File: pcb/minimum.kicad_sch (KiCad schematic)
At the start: 32 parts, among them J1 DX07P024MJ1R1500, J2 Conn_01x02, U1 RP2040, U2 SCD4x, U3 W25Q16JVUXIQ, U4 XCL220, Y1 C2E-12.000-18-1020-X-R

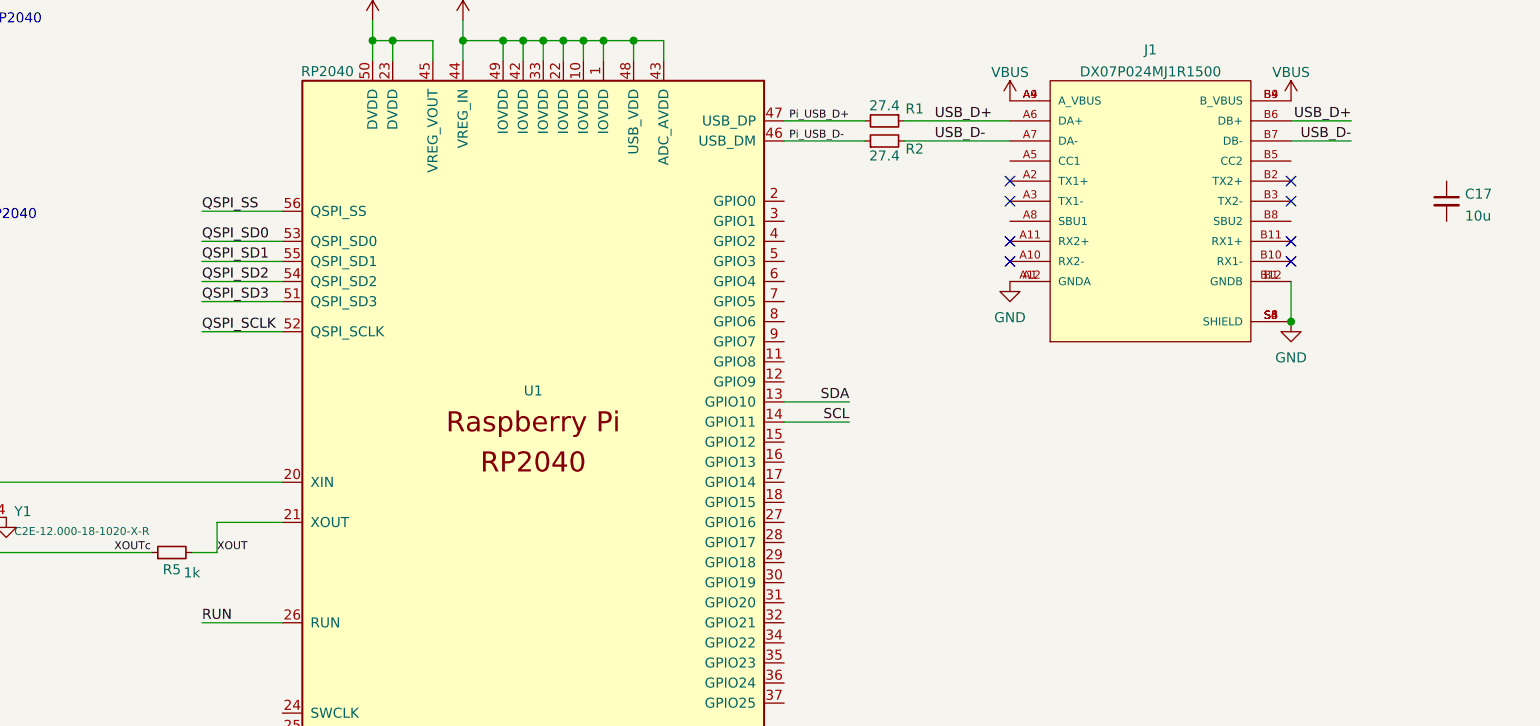
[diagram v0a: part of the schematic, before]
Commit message: routing VBUS
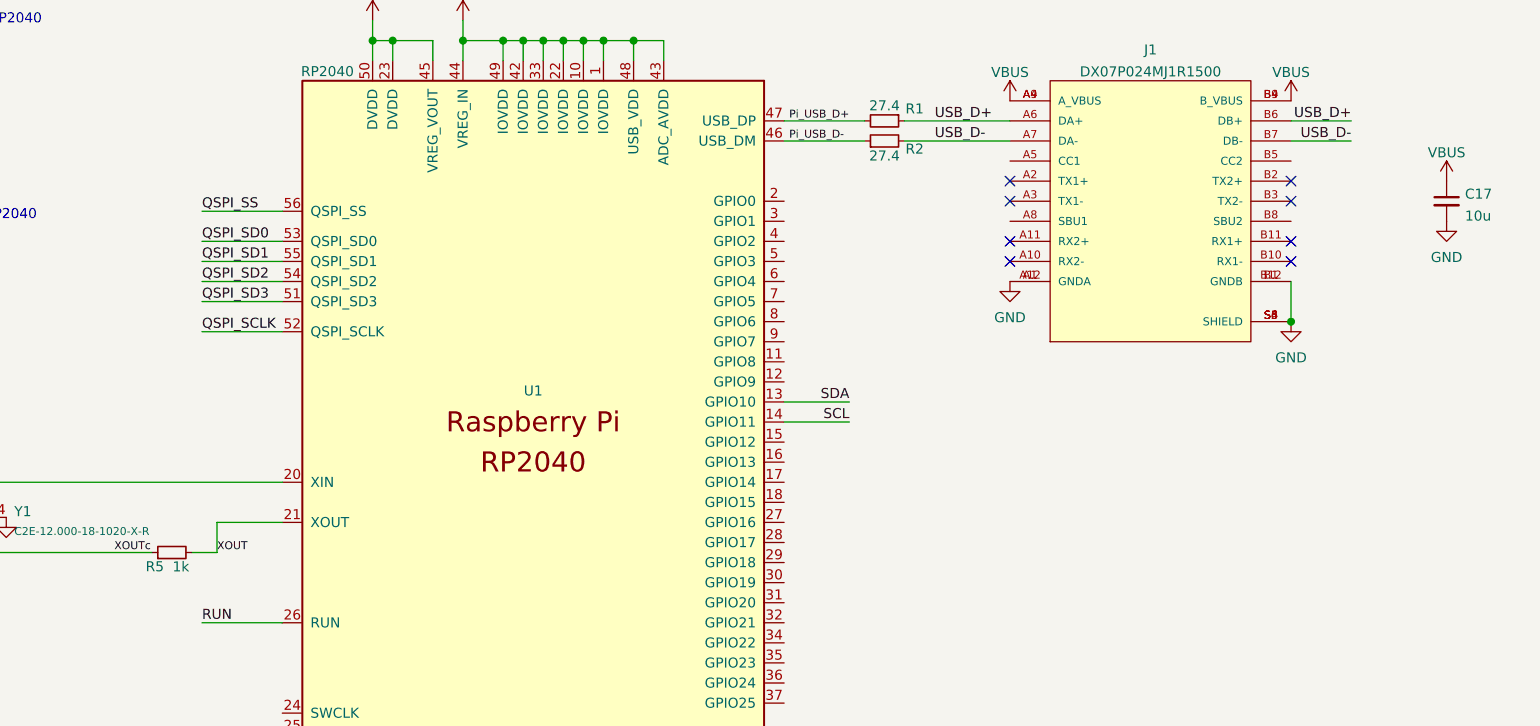
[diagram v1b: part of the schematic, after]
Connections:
- net GND: now also C17.2
- net VBUS: now also C17.1
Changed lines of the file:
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@@
   (symbol (lib_id "power:VBUS") (at 273.05 175.895 0) (unit 1)
     (in_bom yes) (on_board yes) (fields_autoplaced)
-    (property "Reference" "#PWR?" (id 0) (at 273.05 179.705 0)
+    (property "Reference" "#PWR0127" (id 0) (at 273.05 179.705 0)
       (effects (font (size 1.27 1.27)) hide)
     )
@@
     (pin "1")
   )
+  (symbol (lib_id "power:VBUS") (at 295.91 46.355 0) (unit 1)
+    (in_bom yes) (on_board yes) (fields_autoplaced)
+    (property "Reference" "#PWR?" (id 0) (at 295.91 50.165 0)
+      (effects (font (size 1.27 1.27)) hide)
+    )
+    (property "Value" "VBUS" (id 1) (at 295.91 42.7504 0))
+    (property "Footprint" "" (id 2) (at 295.91 46.355 0)
+      (effects (font (size 1.27 1.27)) hide)
+    )
+    (property "Datasheet" "" (id 3) (at 295.91 46.355 0)
+      (effects (font (size 1.27 1.27)) hide)
+    )
+    (pin "1")
+  )
   (symbol (lib_id "power:+3V3") (at 298.958 189.23 0) (unit 1)
     (in_bom yes) (on_board yes) (fields_autoplaced)
@@
     )
     (property "Datasheet" "" (id 3) (at 276.225 64.135 0)
+      (effects (font (size 1.27 1.27)) hide)
+    )
+    (pin "1")
+  )
+  (symbol (lib_id "power:GND") (at 295.91 51.435 0) (unit 1)
+    (in_bom yes) (on_board yes) (fields_autoplaced)
+    (property "Reference" "#PWR?" (id 0) (at 295.91 57.785 0)
+      (effects (font (size 1.27 1.27)) hide)
+    )
+    (property "Value" "GND" (id 1) (at 295.91 55.9976 0))
+    (property "Footprint" "" (id 2) (at 295.91 51.435 0)
+      (effects (font (size 1.27 1.27)) hide)
+    )
+    (property "Datasheet" "" (id 3) (at 295.91 51.435 0)
       (effects (font (size 1.27 1.27)) hide)
     )
@@
   (symbol (lib_id "Device:R_Small") (at 134.62 93.345 90) (unit 1)
     (in_bom yes) (on_board yes)
-    (property "Reference" "R5" (id 0) (at 134.62 95.5082 90))
-    (property "Value" "1k" (id 1) (at 137.16 95.9081 90))
+    (property "Reference" "R5" (id 0) (at 132.461 95.1272 90))
+    (property "Value" "1k" (id 1) (at 135.763 95.1461 90))
     (property "Footprint" "Resistor_SMD:R_0402_1005Metric" (id 2) (at 134.62 93.345 0)
       (effects (font (size 1.27 1.27)) hide)
@@
       (reference "#PWR0126") (unit 1) (value "+3V3") (footprint "")
     )
+    (path "/fbe7173c-3624-4a8e-9ddc-41f9ad3603b0"
+      (reference "#PWR0127") (unit 1) (value "VBUS") (footprint "")
+    )
     (path "/6f6d4540-ef37-47a0-98e2-40a1cdda8c1c"
       (reference "#PWR0128") (unit 1) (value "GND") (footprint "")
@@
       (reference "#PWR0132") (unit 1) (value "GND") (footprint "")
     )
-    (path "/fbe7173c-3624-4a8e-9ddc-41f9ad3603b0"
+    (path "/07335941-1864-4a66-b2dd-cc5d4e9a1d22"
+      (reference "#PWR?") (unit 1) (value "GND") (footprint "")
+    )
+    (path "/3e1adbd0-e23c-433f-bc25-4fa06fc8e9a6"
       (reference "#PWR?") (unit 1) (value "VBUS") (footprint "")
     )

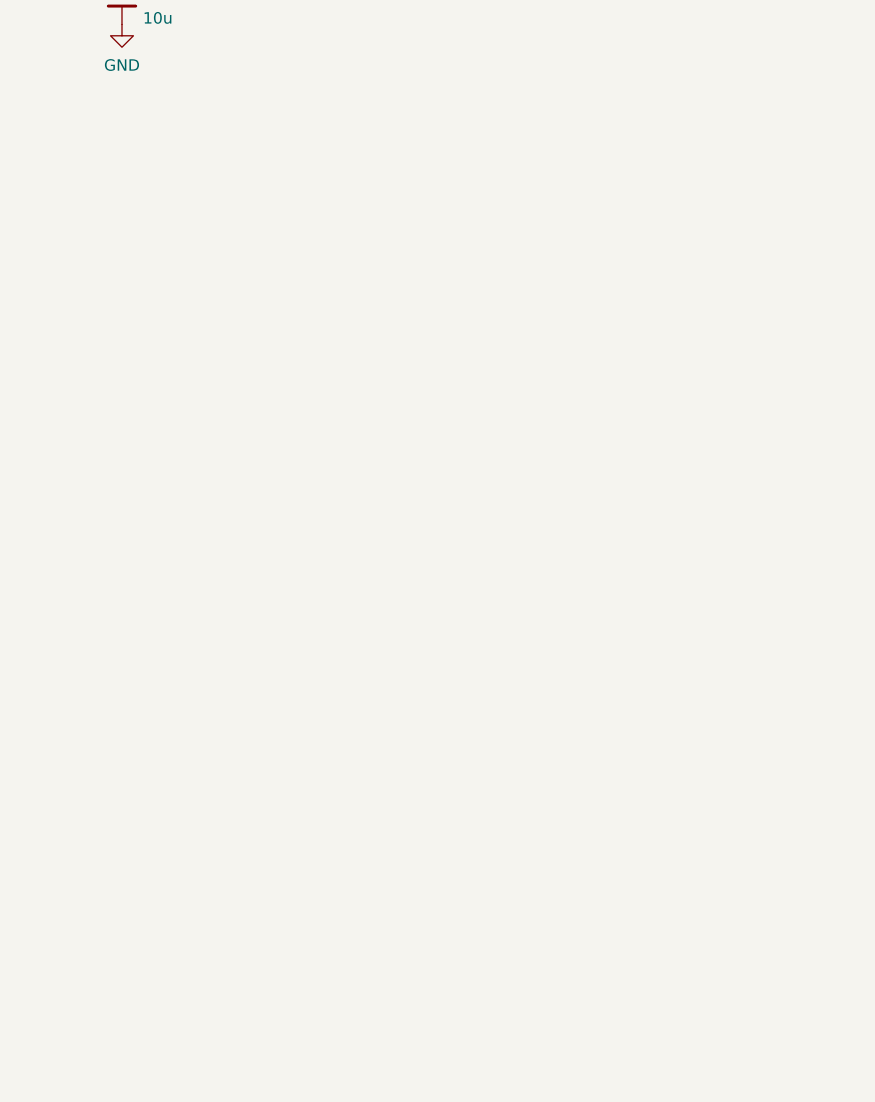
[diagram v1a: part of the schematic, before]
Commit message: adding led and push button libs
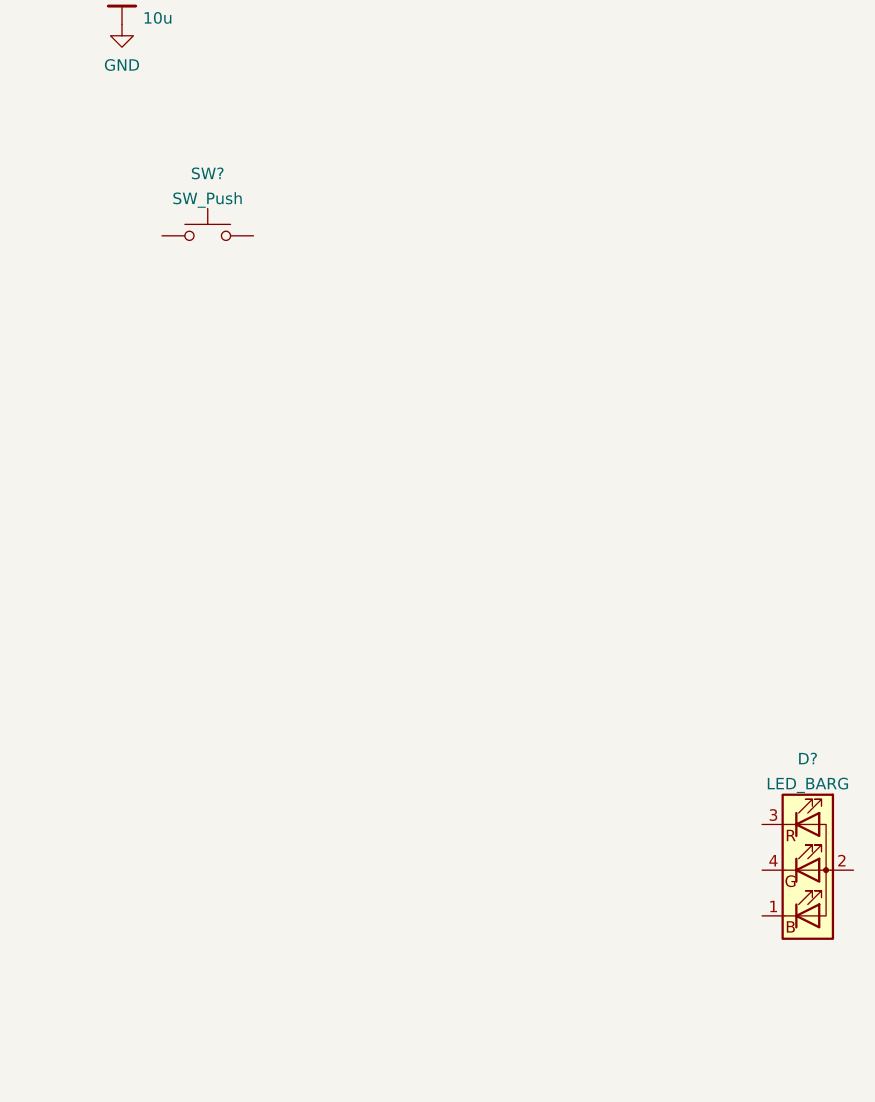
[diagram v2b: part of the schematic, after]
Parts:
- added D?: LED_BARG, symbol Device:LED_BARG
- added SW?: SW_Push, symbol Switch:SW_Push
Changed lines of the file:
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@@
+    (pin "2")
+  )
+  (symbol (lib_id "Switch:SW_Push") (at 305.435 74.93 0) (unit 1)
+    (in_bom yes) (on_board yes) (fields_autoplaced)
+    (property "Reference" "SW?" (id 0) (at 305.435 68.0424 0))
+    (property "Value" "SW_Push" (id 1) (at 305.435 70.8175 0))
+    (property "Footprint" "" (id 2) (at 305.435 69.85 0)
+      (effects (font (size 1.27 1.27)) hide)
+    )
+    (property "Datasheet" "~" (id 3) (at 305.435 69.85 0)
+      (effects (font (size 1.27 1.27)) hide)
+    )
+    (pin "1")
     (pin "2")
   )
@@
     )
     (property "Manufacturer Product Number" "C2E-12.000-18-1020-X-R" (id 4) (at 108.585 88.9 0)
+      (effects (font (size 1.27 1.27)) hide)
+    )
+    (pin "1")
+    (pin "2")
+    (pin "3")
+    (pin "4")
+  )
+  (symbol (lib_id "Device:LED_BARG") (at 372.11 145.415 0) (unit 1)
+    (in_bom yes) (on_board yes) (fields_autoplaced)
+    (property "Reference" "D?" (id 0) (at 372.11 133.0664 0))
+    (property "Value" "LED_BARG" (id 1) (at 372.11 135.8415 0))
+    (property "Footprint" "" (id 2) (at 372.11 146.685 0)
+      (effects (font (size 1.27 1.27)) hide)
+    )
+    (property "Datasheet" "~" (id 3) (at 372.11 146.685 0)
       (effects (font (size 1.27 1.27)) hide)
     )
@@
       (reference "C18") (unit 1) (value "10u") (footprint "Capacitor_SMD:C_0603_1608Metric")
     )
+    (path "/d2662a96-3c28-4da6-abf3-32210a6a0d2d"
+      (reference "D?") (unit 1) (value "LED_BARG") (footprint "")
+    )
     (path "/055c229d-49d0-4802-a7e2-2793179f3436"
       (reference "J1") (unit 1) (value "DX07P024MJ1R1500") (footprint "SMD:JAE_DX07P024MJ1R1500")
@@
       (reference "R7") (unit 1) (value "10k") (footprint "Resistor_SMD:R_0402_1005Metric")
     )
+    (path "/2c757bb5-a52b-489f-818b-771ac8ceb9d1"
+      (reference "SW?") (unit 1) (value "SW_Push") (footprint "")
+    )
     (path "/650359b7-067b-40bd-8aa7-4d9b211abef0"

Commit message: routing
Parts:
- removed J2: Conn_01x02, symbol Connector_Generic:Conn_01x02
- added R10, R8, R9: 470, Resistor_SMD:R_0402_1005Metric, symbol Device:R_Small
- D1: renamed from D?; footprint (none) -> SMD:RGB_LED_3x1
- SW1: renamed from SW?; footprint (none) -> SMD:TL3340AF160QG
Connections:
- net GND: now also D1.2 (A), SW1.1
- net at SW1.2: now also R6.1
- net LED_B: now reaches U1.32 (GPIO21)
- net LED_B: now also R10.1
- net LED_R: now reaches U1.34 (GPIO22)
- net LED_R: now also R8.1
- net LED_G: now reaches U1.35 (GPIO23)
- net LED_G: now also R9.1
- net at D1.1 (BK): now also R10.2
- net at D1.3 (RK): now also R8.2
- net at D1.4 (GK): now also R9.2
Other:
- moved on the sheet: SW1

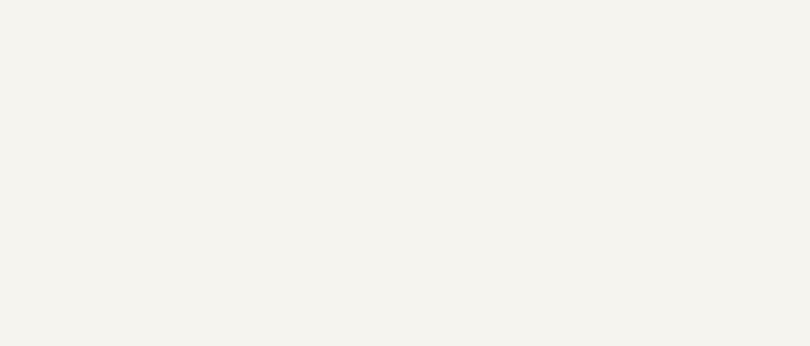
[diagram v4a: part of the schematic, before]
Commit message: OH logo added
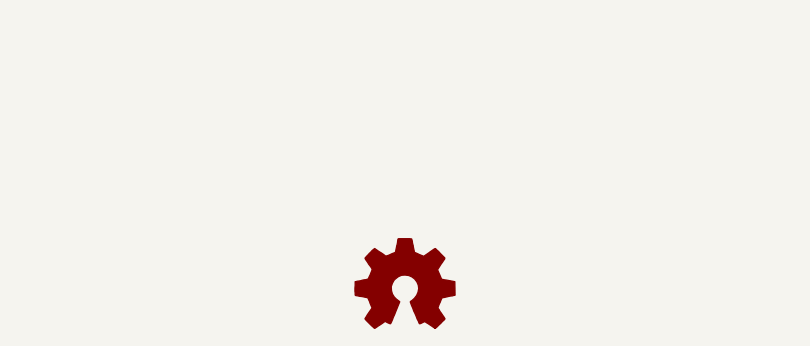
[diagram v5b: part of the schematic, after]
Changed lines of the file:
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@@
     (pin "4")
+  )
+  (symbol (lib_id "Graphic:Logo_Open_Hardware_Small") (at 283.21 254 0) (unit 1)
+    (in_bom yes) (on_board yes) (fields_autoplaced)
+    (property "Reference" "#LOGO1" (id 0) (at 283.21 247.015 0)
+      (effects (font (size 1.27 1.27)) hide)
+    )
+    (property "Value" "Logo_Open_Hardware_Small" (id 1) (at 283.21 259.715 0)
+      (effects (font (size 1.27 1.27)) hide)
+    )
+    (property "Footprint" "Symbol:OSHW-Logo_5.7x6mm_SilkScreen" (id 2) (at 283.21 254 0)
+      (effects (font (size 1.27 1.27)) hide)
+    )
+    (property "Datasheet" "~" (id 3) (at 283.21 254 0)
+      (effects (font (size 1.27 1.27)) hide)
+    )
   )
   (symbol (lib_id "Device:LED_BARG") (at 372.11 145.415 0) (unit 1)
@@
   )
   (symbol_instances
+    (path "/301d137e-e414-44ec-b59d-d2017fb2304d"
+      (reference "#LOGO1") (unit 1) (value "Logo_Open_Hardware_Small") (footprint "Symbol:OSHW-Logo_5.7x6mm_SilkScreen")
+    )
     (path "/1fbc932d-28dd-4b95-9e32-a7b700db5124"
       (reference "#PWR0101") (unit 1) (value "GND") (footprint "")

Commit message: changing the USB connector following the recommendation of arturo182
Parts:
- J1: footprint SMD:JAE_DX07P024MJ1R1500 -> SMD:USB_C_Plug_UTC009-C12
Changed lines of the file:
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@@
     (property "Reference" "J1" (id 0) (at 258.445 29.7392 0))
     (property "Value" "DX07P024MJ1R1500" (id 1) (at 258.445 32.5143 0))
-    (property "Footprint" "SMD:JAE_DX07P024MJ1R1500" (id 2) (at 258.445 51.435 0)
+    (property "Footprint" "SMD:USB_C_Plug_UTC009-C12" (id 2) (at 258.445 51.435 0)
       (effects (font (size 1.27 1.27)) (justify left bottom) hide)
     )
@@
     )
     (path "/055c229d-49d0-4802-a7e2-2793179f3436"
-      (reference "J1") (unit 1) (value "DX07P024MJ1R1500") (footprint "SMD:JAE_DX07P024MJ1R1500")
+      (reference "J1") (unit 1) (value "DX07P024MJ1R1500") (footprint "SMD:USB_C_Plug_UTC009-C12")
     )
     (path "/6560932e-72e1-448b-b0e8-fca0e2461287"

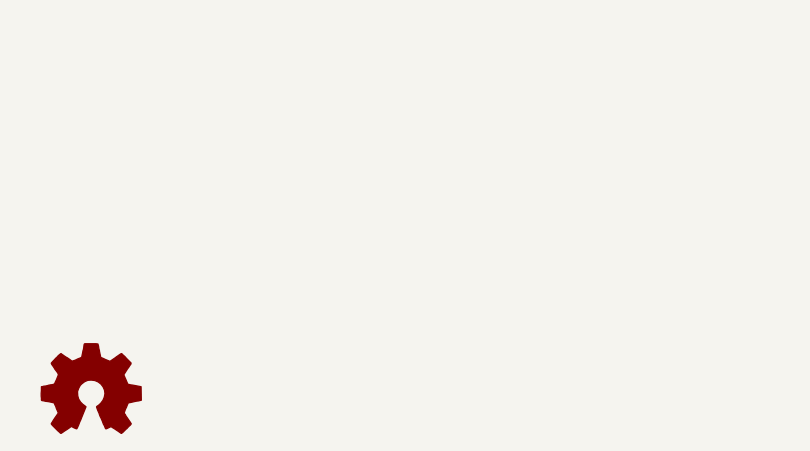
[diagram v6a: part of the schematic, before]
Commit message: OpenHardware logo added
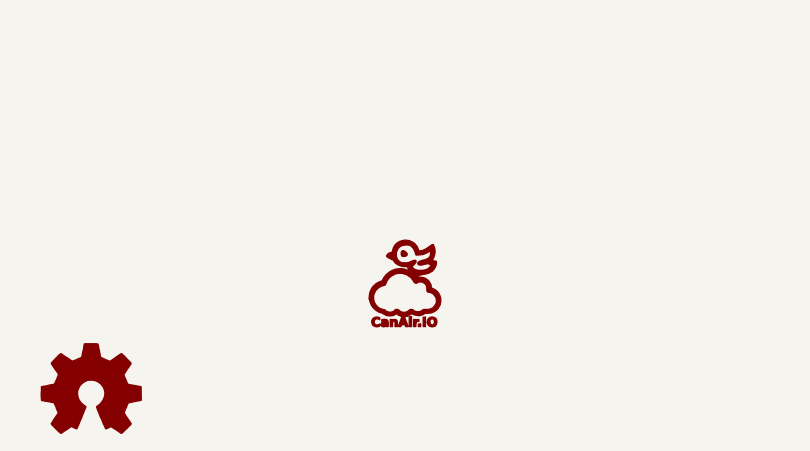
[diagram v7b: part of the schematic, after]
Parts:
- added LOGO1: LOGO, SMD:CanAir_IO, symbol CanAir_IO:LOGO
- added LOGO2: Logo_Open_Hardware_Small, Symbol:OSHW-Symbol_6.7x6mm_SilkScreen, symbol Graphic:Logo_Open_Hardware_Small
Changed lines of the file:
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@@
     (pin "2")
+  )
+  (symbol (lib_id "CanAir_IO:LOGO") (at 318.135 241.3 0) (unit 1)
+    (in_bom yes) (on_board yes) (fields_autoplaced)
+    (property "Reference" "LOGO1" (id 0) (at 318.135 245.8466 0)
+      (effects (font (size 1.27 1.27)) hide)
+    )
+    (property "Value" "LOGO" (id 1) (at 318.135 236.7534 0)
+      (effects (font (size 1.27 1.27)) hide)
+    )
+    (property "Footprint" "SMD:CanAir_IO" (id 2) (at 318.135 241.3 0)
+      (effects (font (size 1.27 1.27)) hide)
+    )
+    (property "Datasheet" "" (id 3) (at 318.135 241.3 0)
+      (effects (font (size 1.27 1.27)) hide)
+    )
   )
   (symbol (lib_id "Device:Crystal_GND24") (at 108.585 88.9 90) (unit 1)
@@
   (symbol (lib_id "Graphic:Logo_Open_Hardware_Small") (at 283.21 254 0) (unit 1)
     (in_bom yes) (on_board yes) (fields_autoplaced)
-    (property "Reference" "#LOGO1" (id 0) (at 283.21 247.015 0)
+    (property "Reference" "LOGO2" (id 0) (at 283.21 247.015 0)
       (effects (font (size 1.27 1.27)) hide)
     )
@@
       (effects (font (size 1.27 1.27)) hide)
     )
-    (property "Footprint" "Symbol:OSHW-Logo_5.7x6mm_SilkScreen" (id 2) (at 283.21 254 0)
+    (property "Footprint" "Symbol:OSHW-Symbol_6.7x6mm_SilkScreen" (id 2) (at 283.21 254 0)
       (effects (font (size 1.27 1.27)) hide)
     )
@@
   )
   (symbol_instances
-    (path "/301d137e-e414-44ec-b59d-d2017fb2304d"
-      (reference "#LOGO1") (unit 1) (value "Logo_Open_Hardware_Small") (footprint "Symbol:OSHW-Logo_5.7x6mm_SilkScreen")
-    )
     (path "/1fbc932d-28dd-4b95-9e32-a7b700db5124"
       (reference "#PWR0101") (unit 1) (value "GND") (footprint "")
@@
       (reference "J1") (unit 1) (value "DX07P024MJ1R1500") (footprint "SMD:USB_C_Plug_UTC009-C12")
     )
+    (path "/0a39c883-d901-4647-8da4-adc87839bedc"
+      (reference "LOGO1") (unit 1) (value "LOGO") (footprint "SMD:CanAir_IO")
+    )
+    (path "/301d137e-e414-44ec-b59d-d2017fb2304d"
+      (reference "LOGO2") (unit 1) (value "Logo_Open_Hardware_Small") (footprint "Symbol:OSHW-Symbol_6.7x6mm_SilkScreen")
+    )
     (path "/6560932e-72e1-448b-b0e8-fca0e2461287"

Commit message: useless fixes :/
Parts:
- LOGO2: footprint Symbol:OSHW-Symbol_6.7x6mm_SilkScreen -> SMD:OHW_LOGO
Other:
- moved on the sheet: C16, C18, C8, C9, D1, R10, R3, R4, R6, R7, R8, R9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
